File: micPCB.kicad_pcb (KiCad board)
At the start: 2 copper layers, 16 x 16 mm, 7 parts, among them J1 Conn_01x02, J2 Conn_01x03, J3 Conn_01x02, U1 ADAU7002

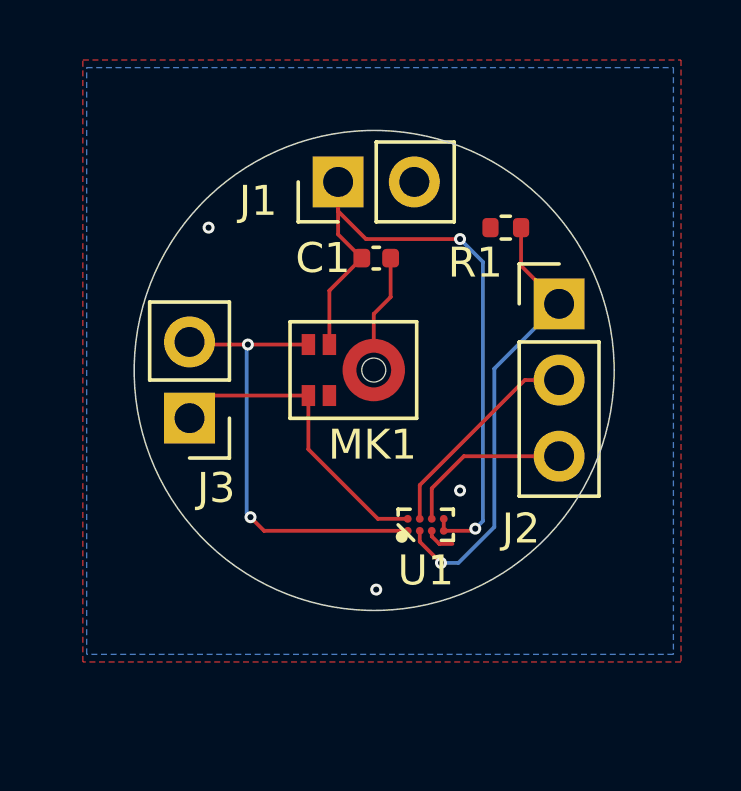
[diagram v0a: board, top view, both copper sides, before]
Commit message: fixed all github issues except bom. Moved headers inwarts. Widened tracks and added fiducels
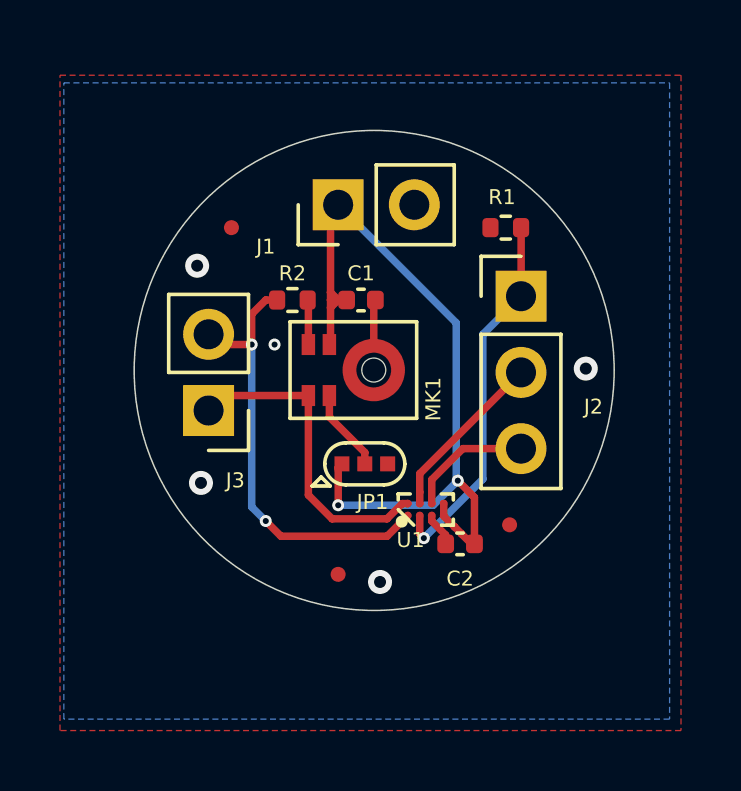
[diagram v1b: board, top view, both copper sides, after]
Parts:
- added C2: 0.1uF, Capacitor_SMD:C_0402_1005Metric, F.Cu at (120.4, 98.0)
- added JP1: SolderJumper_3_Open, custom:SolderJumper-3_P0.635mm_Open_RoundedPad1.0x1.5mm, F.Cu at (117.2, 95.4)
- added R2: 100, Resistor_SMD:R_0402_1005Metric, F.Cu at (114.8, 89.9)
- added REF**: Fiducial_0.5mm_Mask1mm, Fiducial:Fiducial_0.5mm_Mask1mm, F.Cu at (116.3, 99.1)
- added REF**: Fiducial_0.5mm_Mask1mm, Fiducial:Fiducial_0.5mm_Mask1mm, F.Cu at (122.0, 97.4)
- added REF**: Fiducial_0.5mm_Mask1mm, Fiducial:Fiducial_0.5mm_Mask1mm, F.Cu at (112.8, 87.5)
- C1: value 0.1uF -> 100nF
- moved C1 1.49 mm to (117.1, 89.9)
- moved J2 1.30 mm to (122.4, 89.8)
- moved J1 0.76 mm to (116.3, 86.7)
- moved J3 0.68 mm to (112.0, 93.6)
- moved U1 0.51 mm to (119.3, 96.9)
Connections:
- MK1 pad 1: /PDM_DAT -> Net-(MK1-Pad1)
- MK1 pad 4: GND -> /LRSELECT
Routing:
- net VDD: track 23.2 -> 26.5 mm
- net /LRSELECT: track 0.00 -> 2.77 mm
- net /SDATA: track 15.0 -> 12.5 mm
- net /LRCLK: track 5.70 -> 4.20 mm
- net Net-(MK1-Pad1): track 0.00 -> 1.49 mm
- net /BCLK: track 7.22 -> 5.77 mm
- net /PDM_CLK: track 10.3 -> 11.4 mm
- net GND: track 4.43 -> 4.31 mm, vias 3 -> 5
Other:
- net class small: trace_width 0.127 -> 0.25
- board text added: "Klankentappers V 1.0"
